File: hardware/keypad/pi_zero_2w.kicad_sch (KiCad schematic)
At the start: 15 parts, among them Q502 BSS138 JI, U501 NC7SZ08M5X, U503 LMC555CMX/NOPB

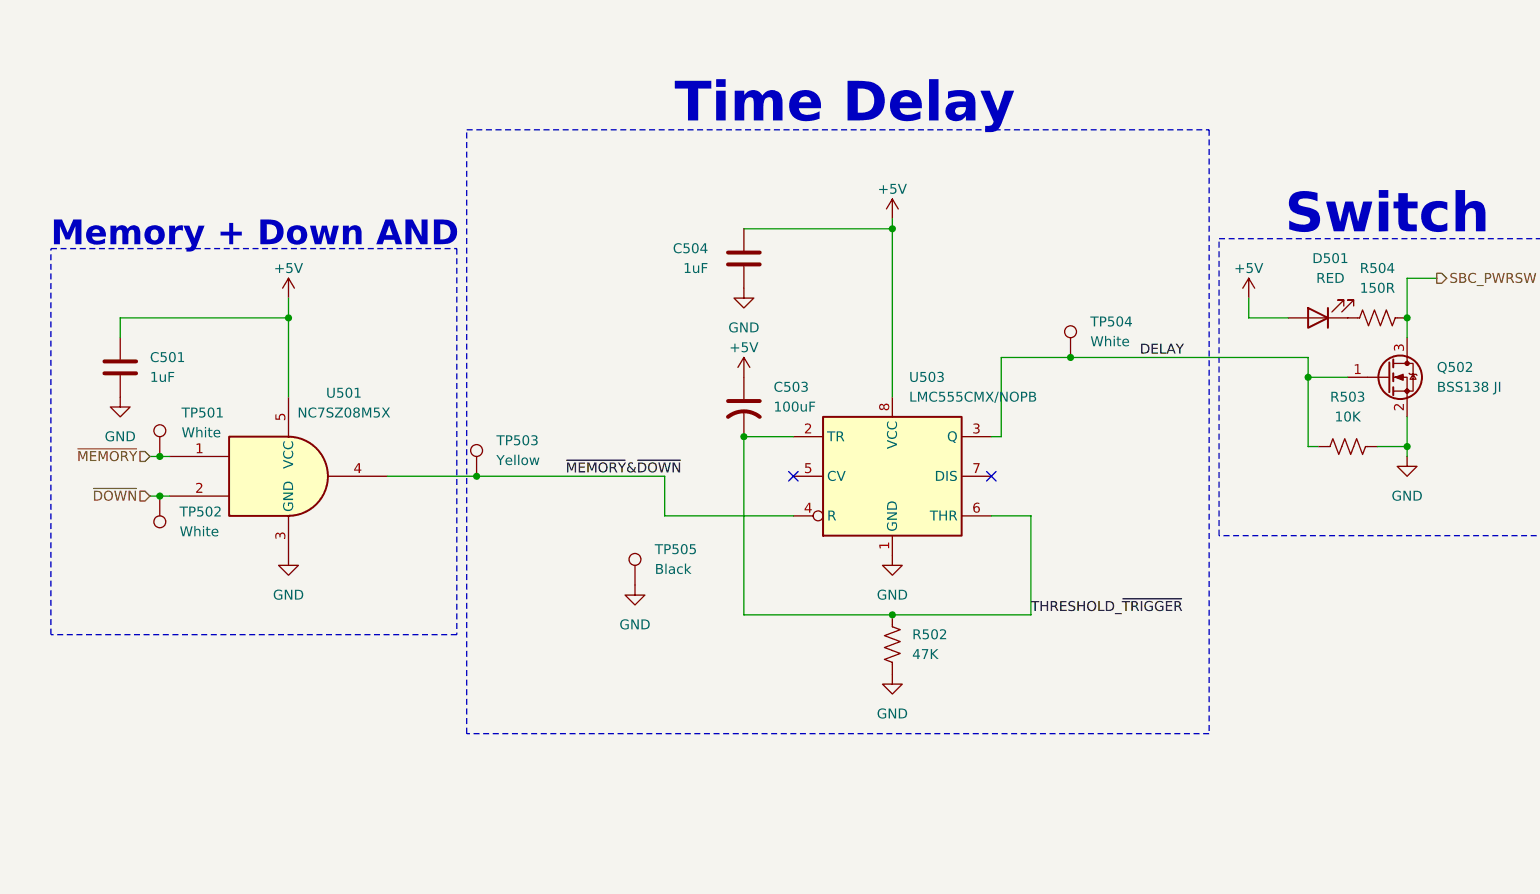
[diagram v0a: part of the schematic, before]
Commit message: [fix] repeater and sbc shutdown circuit
Fixed repeater and SBC shutdown circuit. Switched +5V VCC to +3.3V. Added C211
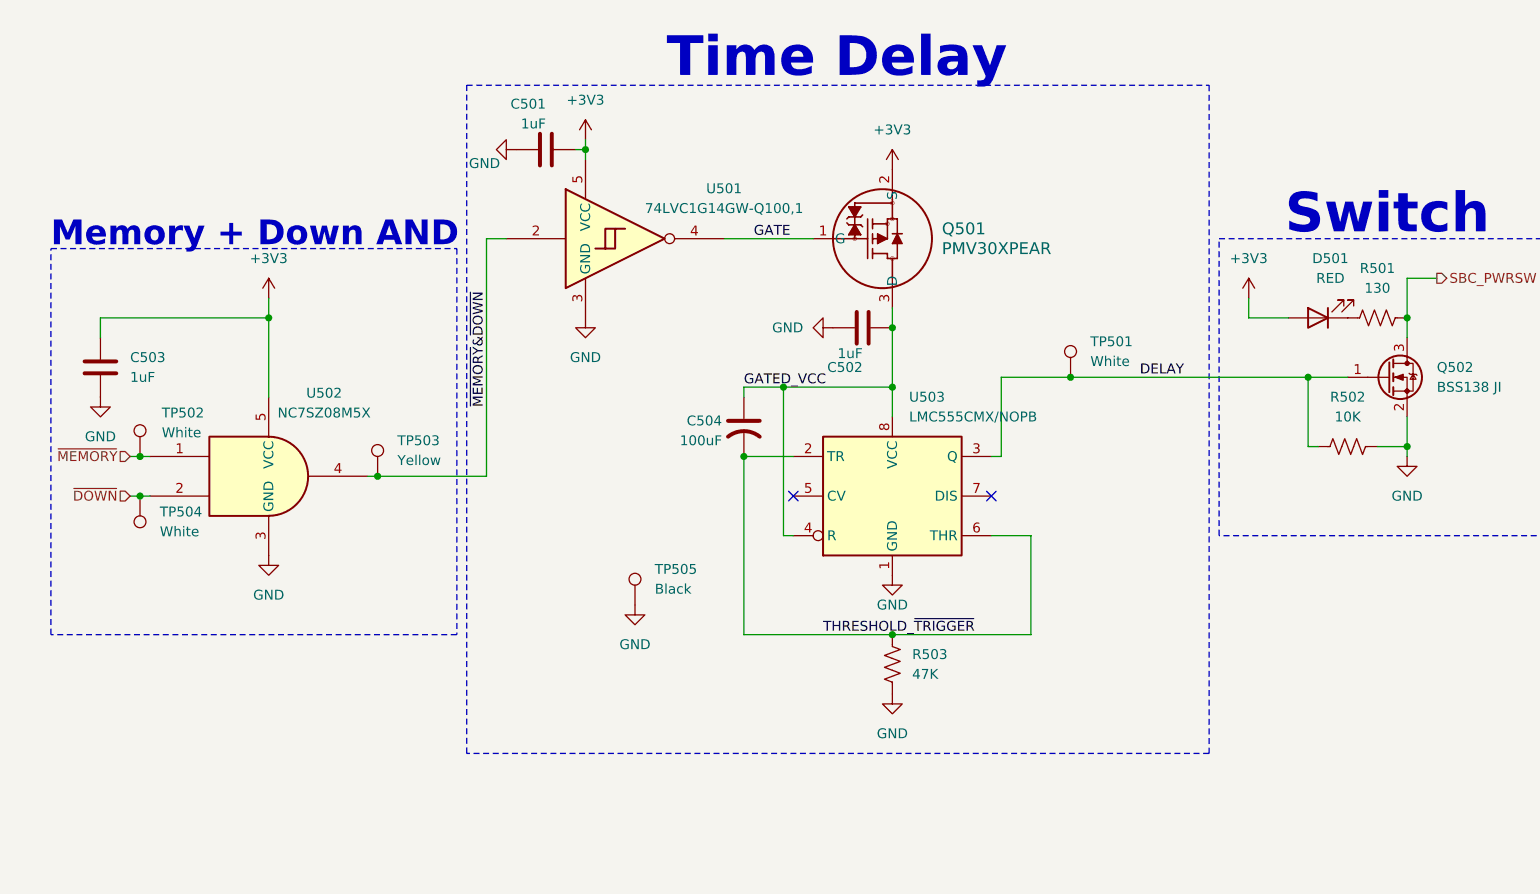
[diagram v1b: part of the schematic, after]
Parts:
- added C501: 1uF, Capacitor_SMD:C_0805_2012Metric, symbol Device:C
- added Q501: PMV30XPEAR, Package_TO_SOT_SMD:SOT-23-3, symbol PMV30XPEA:PMV30XPEAR
- added U501: 74LVC1G14GW-Q100,1, Package_TO_SOT_SMD:SOT-353_SC-70-5, symbol 74xGxx:74AHC1G14
- R501: renamed from R504; value 150R -> 130
- renumbered C504 to C502, C501 to C503, C503 to C504, R503 to R502, R502 to R503, TP504 to TP501, TP501 to TP502, TP502 to TP504, U501 to U502
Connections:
- net GND: now also C501.2, U501.3 (GND)
- net ~{MEMORY}&~{DOWN}: now also U501.2; no longer U503.4 (R)
- net +5V renamed +3V3
- net +3V3: now also C501.1, Q501.2 (S), U501.5 (VCC); no longer C502.1, C504.1, U503.8 (VCC)
- new net GATE: Q501.1 (G), U501.4
- new net GATED_VCC: C502.1, C504.1, Q501.3 (D), U503.4 (R), U503.8 (VCC)
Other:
- moved on the sheet: C502, C503, C504, R503, TP501, TP502, TP503, TP504, TP505, U502, U503
